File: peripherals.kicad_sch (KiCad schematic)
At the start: 28 parts, among them J3 U.FL, U5 nRF24L01P, U6 MPU-6050, U7 M24C02-FMN, Y3 16 MHz

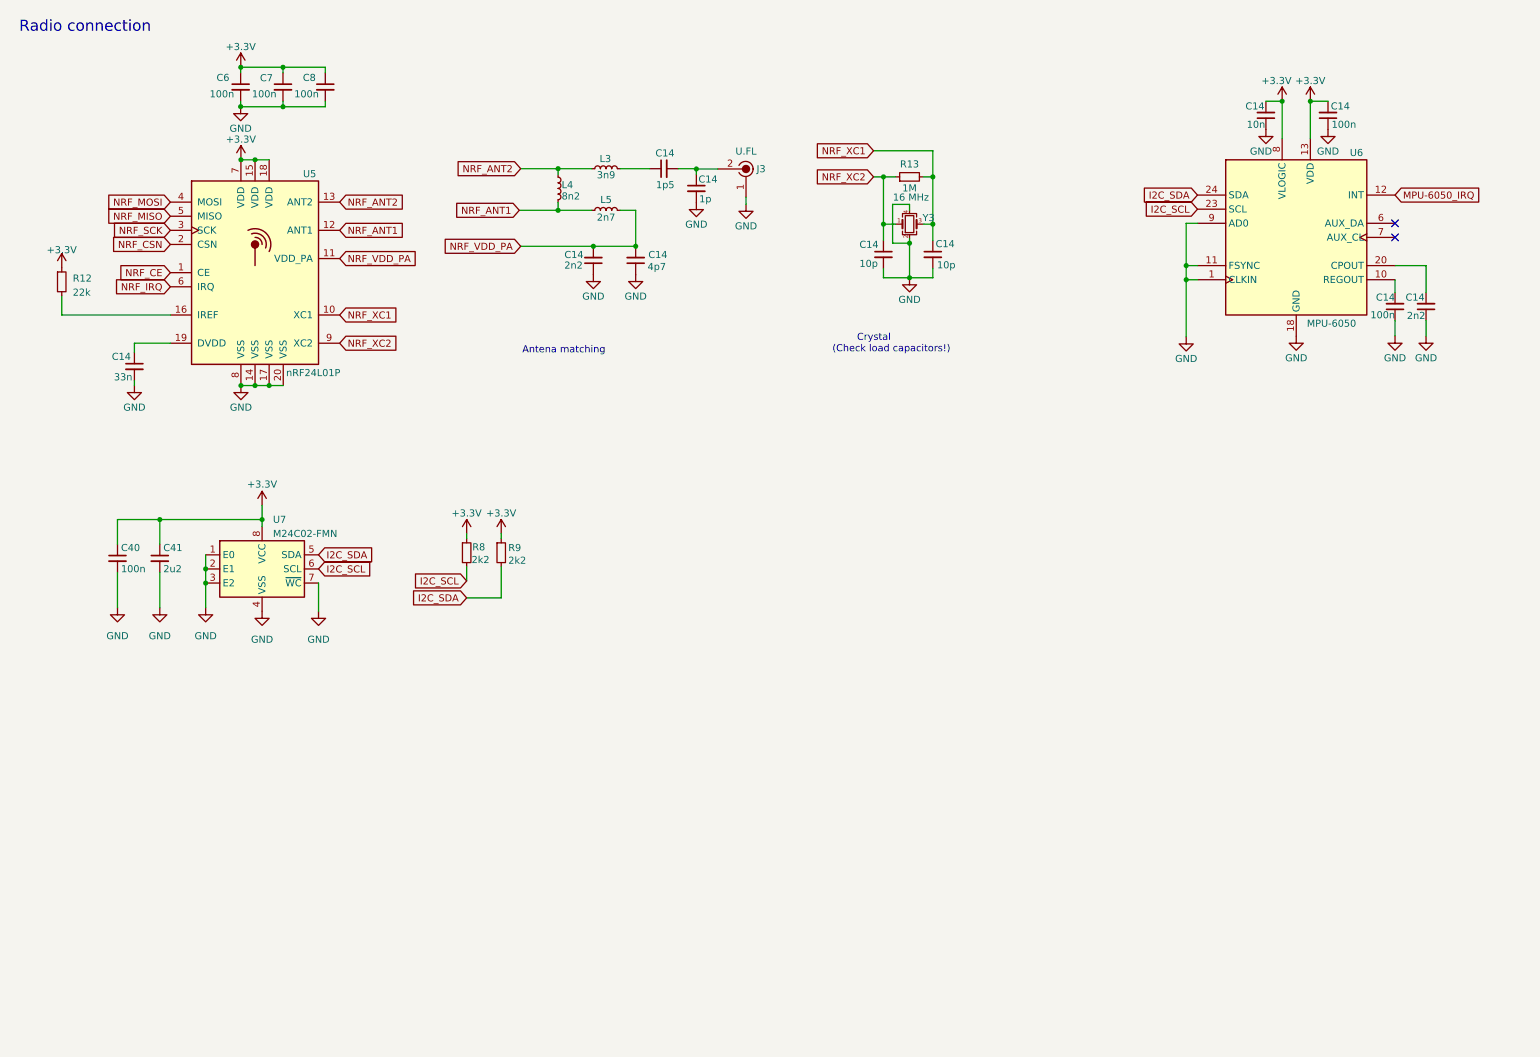
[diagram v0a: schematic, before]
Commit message: most of the components added
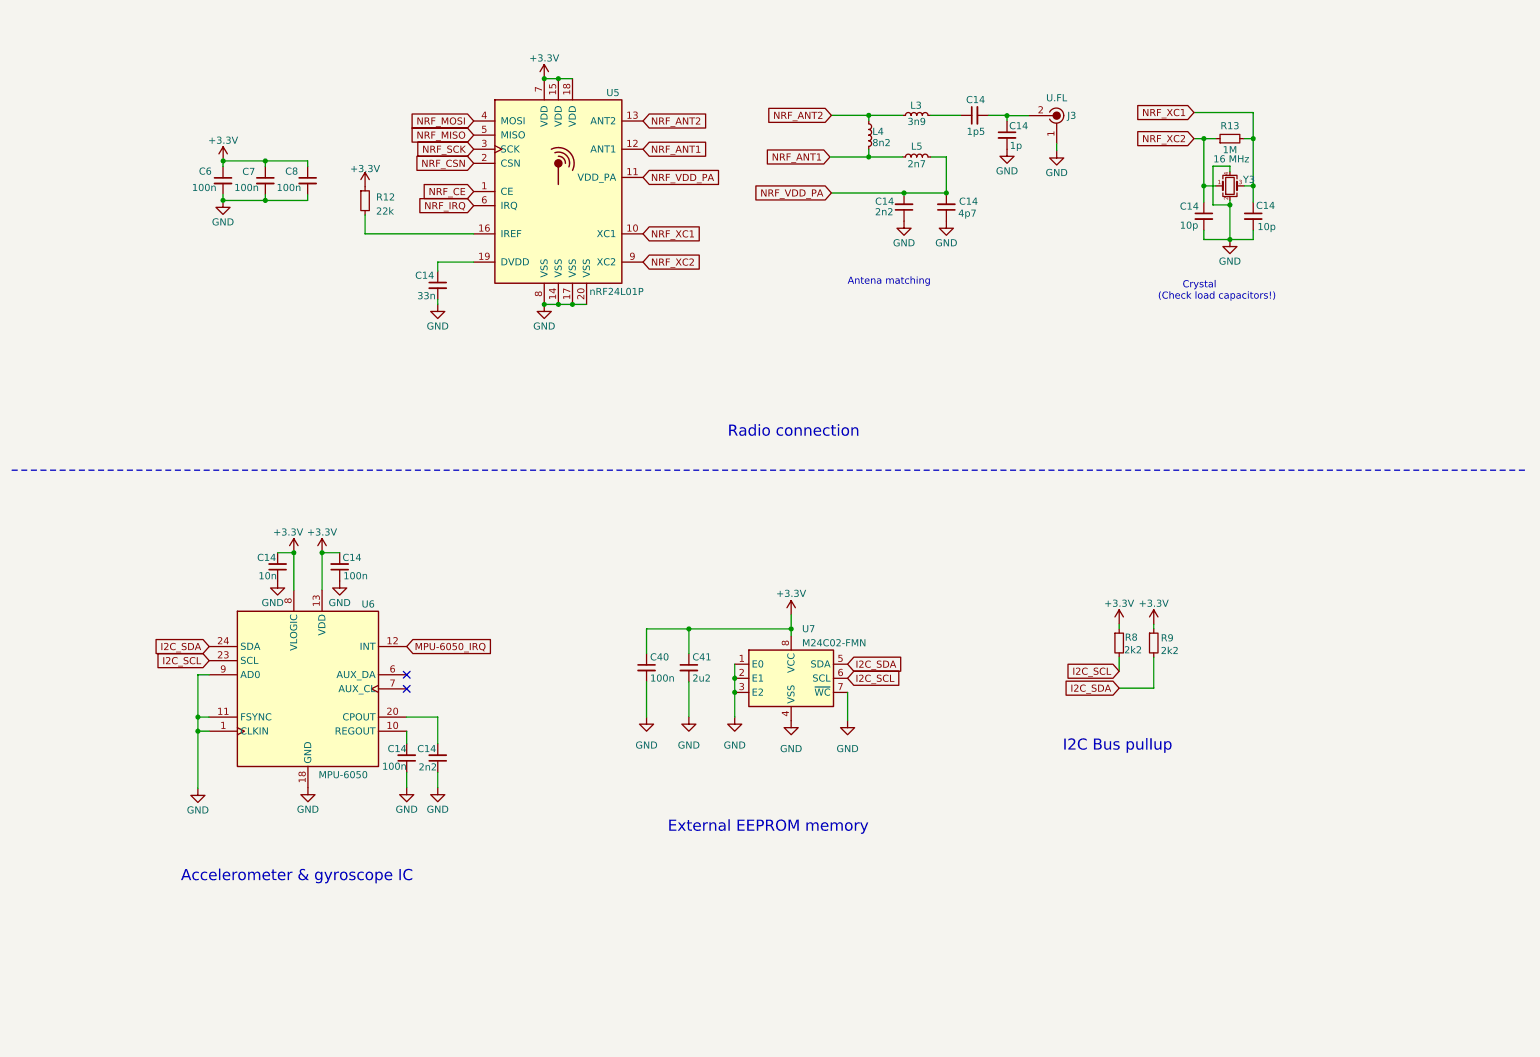
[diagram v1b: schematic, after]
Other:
- note added: "Accelerometer & gyroscope IC"
- note added: "External EEPROM memory"
- note added: "I2C Bus pullup"
- moved on the sheet: C14, C40, C41, C6, C7, C8, J3, L3, L4, L5, R12, R13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

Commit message: schematic completed
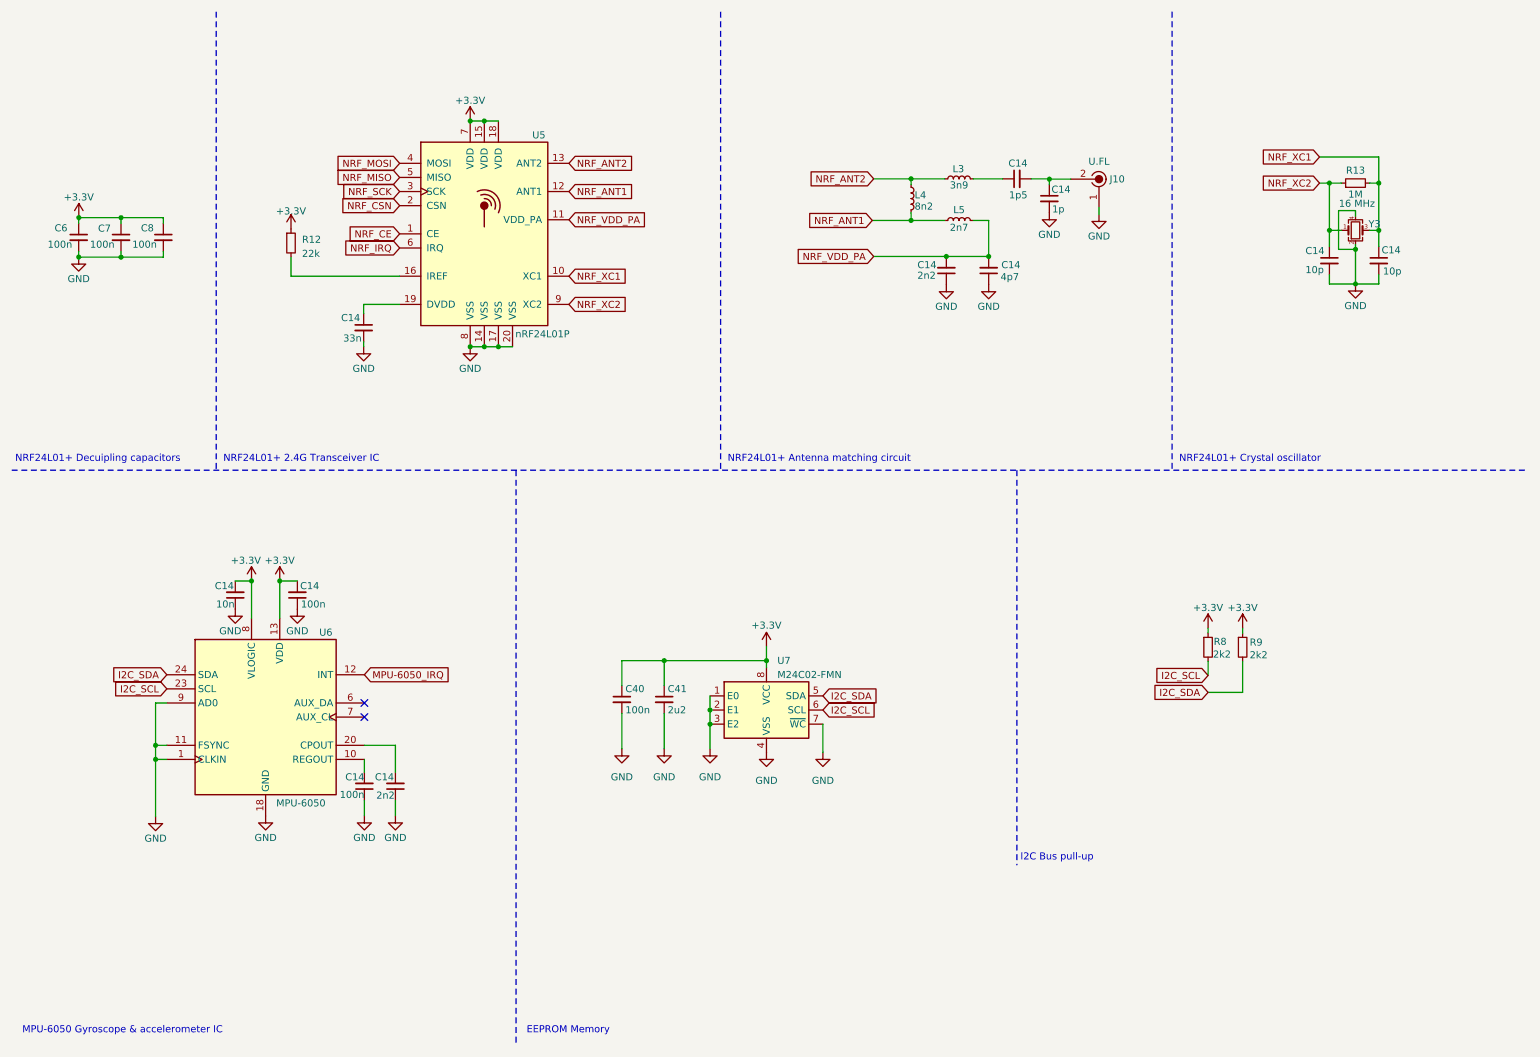
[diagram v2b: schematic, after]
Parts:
- renumbered J3 to J10
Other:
- note added: "EEPROM Memory"
- note added: "I2C Bus pull-up"
- note added: "MPU-6050 Gyroscope & accelerometer IC"
- note added: "NRF24L01+ 2.4G Transceiver IC"
- note added: "NRF24L01+ Antenna matching circuit"
- note added: "NRF24L01+ Crystal oscillator"
- note added: "NRF24L01+ Decuipling capacitors"
- note removed: "Accelerometer & gyroscope IC"
- note removed: "Antena matching"
- note removed: "Crystal (Check load capacitors!)"
- note removed: "External EEPROM memory"
- note removed: "I2C Bus pullup"
- note removed: "Radio connection"
- moved on the sheet: C14, C40, C41, C6, C7, C8, J10, L3, L4, L5, R12, R13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

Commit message: working
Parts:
- C41: footprint Capacitor_SMD:C_1210_3225Metric -> Capacitor_SMD:C_0603_1608Metric

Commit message: working on pcb
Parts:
- C14: footprint Capacitor_SMD:C_0402_1005Metric -> Capacitor_SMD:C_0603_1608Metric
- L3, L4, L5: footprint Inductor_SMD:L_0402_1005Metric -> Inductor_SMD:L_0603_1608Metric

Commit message: layout in progress
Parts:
- C14: footprint Capacitor_SMD:C_0402_1005Metric -> Capacitor_SMD:C_0603_1608Metric

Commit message: layout completed
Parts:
- added TP1: Test MOSI, TestPoint:TestPoint_Pad_D1.0mm, symbol Connector:TestPoint
- added TP2: Test MISO, TestPoint:TestPoint_Pad_D1.0mm, symbol Connector:TestPoint
- added TP3: Test SCK, TestPoint:TestPoint_Pad_D1.0mm, symbol Connector:TestPoint
- added TP4: Test CSN, TestPoint:TestPoint_Pad_D1.0mm, symbol Connector:TestPoint
- added TP5: Test CE, TestPoint:TestPoint_Pad_D1.0mm, symbol Connector:TestPoint
- added TP6: Test IRQ, TestPoint:TestPoint_Pad_D1.0mm, symbol Connector:TestPoint
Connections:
- net NRF_CE: now also TP5.1
- net NRF_CSN: now also TP4.1
- net NRF_IRQ: now also TP6.1
- net NRF_MISO: now also TP2.1
- net NRF_MOSI: now also TP1.1
- net NRF_SCK: now also TP3.1
